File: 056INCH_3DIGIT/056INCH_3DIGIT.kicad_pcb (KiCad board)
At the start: 2 copper layers, 43.8 x 21 mm, 0 parts

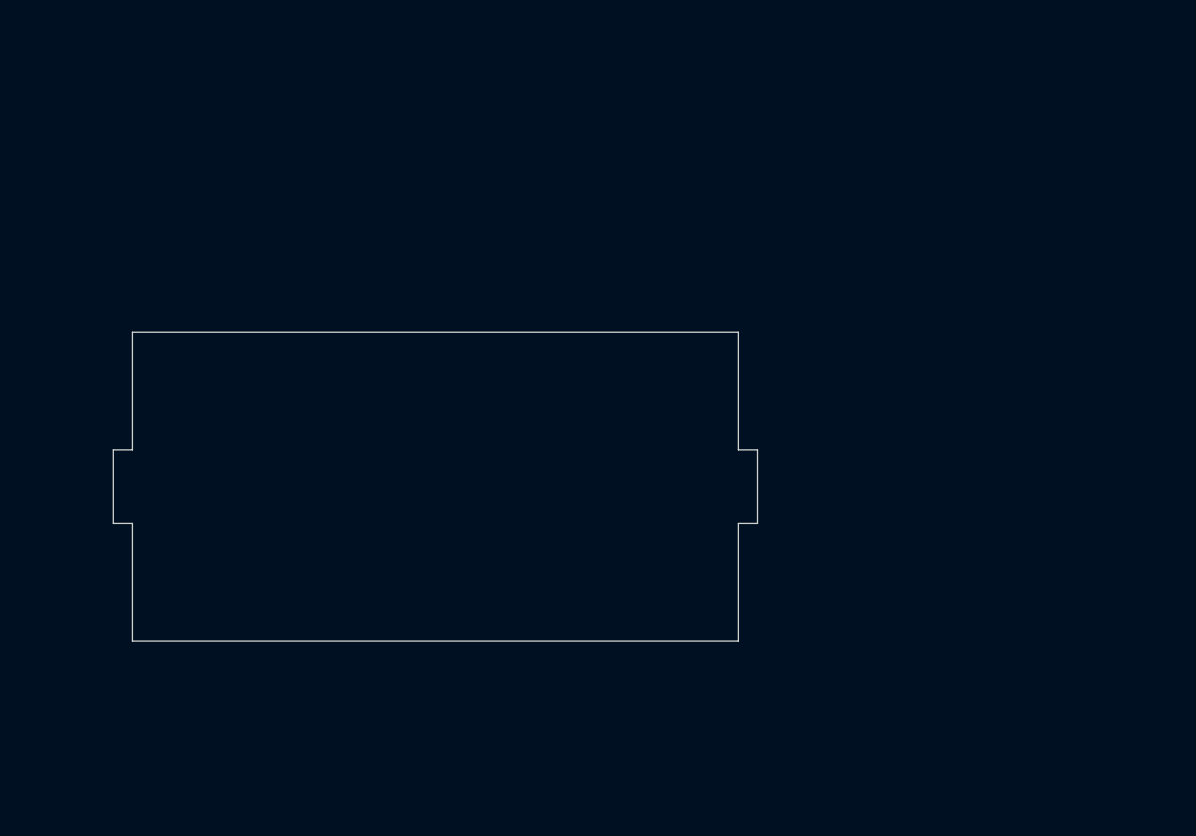
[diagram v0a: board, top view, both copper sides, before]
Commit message: halfway 3 digit display symbol
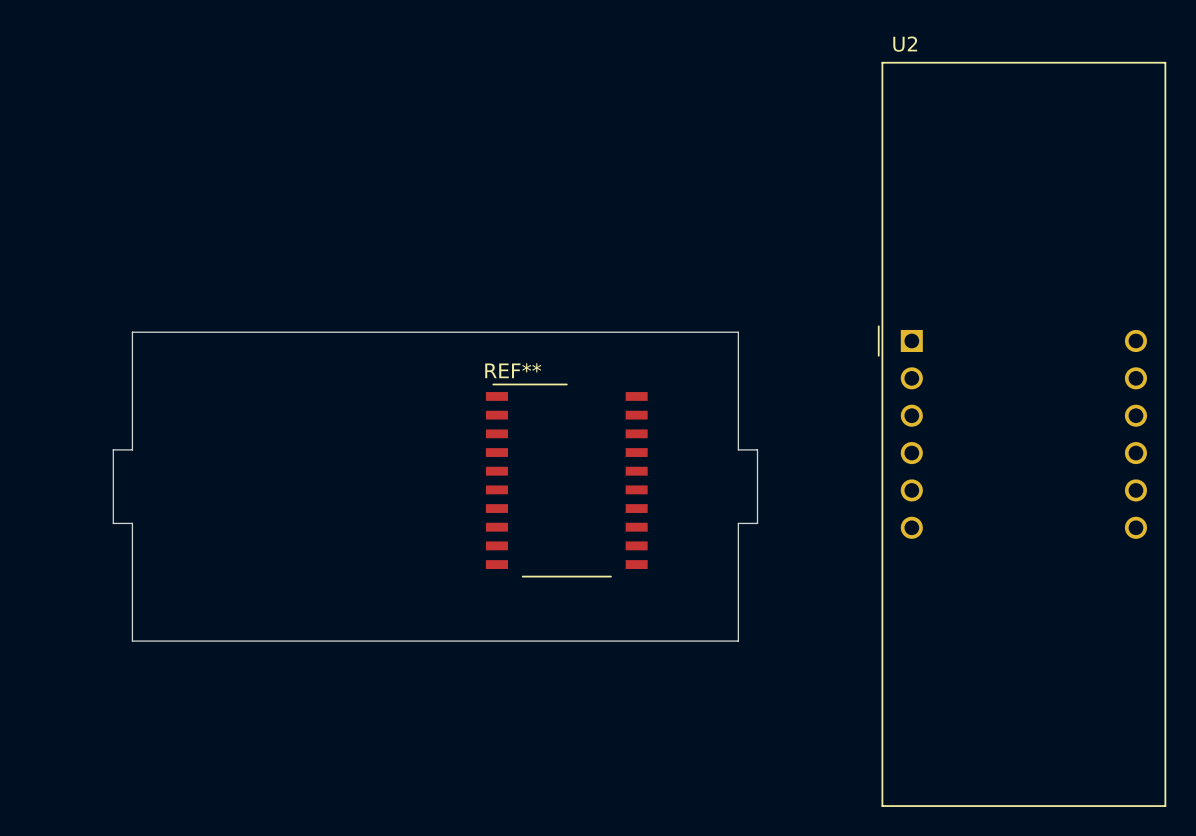
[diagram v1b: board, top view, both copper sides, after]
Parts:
- added REF**: SO-20_12.8x7.5mm_P1.27mm, Package_SO:SO-20_12.8x7.5mm_P1.27mm, F.Cu at (130.8, 110.1)
- added U2: BA56-12SRWA, KINGBRIGHTUSA:BA56-12SRWA, F.Cu at (154.3, 100.6)
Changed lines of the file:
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@@
     (tracks 0)
     (zones 0)
-    (modules 0)
-    (nets 1)
+    (modules 2)
+    (nets 13)
   )
   (page A4)
@@
   )
   (net 0 "")
+  (net 1 "Net-(U2-Pad12)")
+  (net 2 "Net-(U2-Pad11)")
+  (net 3 "Net-(U2-Pad10)")
+  (net 4 "Net-(U2-Pad9)")
+  (net 5 "Net-(U2-Pad8)")
+  (net 6 "Net-(U2-Pad7)")
+  (net 7 "Net-(U2-Pad6)")
+  (net 8 "Net-(U2-Pad5)")
+  (net 9 "Net-(U2-Pad4)")
+  (net 10 "Net-(U2-Pad3)")
+  (net 11 "Net-(U2-Pad2)")
+  (net 12 "Net-(U2-Pad1)")
   (net_class Default "This is the default net class."
     (clearance 0.2)
@@
     (uvia_dia 0.3)
     (uvia_drill 0.1)
+    (add_net "Net-(U2-Pad1)")
+    (add_net "Net-(U2-Pad10)")
+    (add_net "Net-(U2-Pad11)")
+    (add_net "Net-(U2-Pad12)")
+    (add_net "Net-(U2-Pad2)")
+    (add_net "Net-(U2-Pad3)")
+    (add_net "Net-(U2-Pad4)")
+    (add_net "Net-(U2-Pad5)")
+    (add_net "Net-(U2-Pad6)")
+    (add_net "Net-(U2-Pad7)")
+    (add_net "Net-(U2-Pad8)")
+    (add_net "Net-(U2-Pad9)")
+  )
+  (module KINGBRIGHTUSA:BA56-12SRWA (layer F.Cu)
+    (at 154.2923 100.5967)
+    (descr "3 digit 7 segment red LED, https://www.kingbrightusa.com/images/catalog/SPEC/BA56-12SRWA.pdf")
+    (tags "3 digit 7 segment red LED")
+    (fp_text reference U2 (at -0.44 -20.15) (layer F.SilkS)
+      (effects (font (size 1 1) (thickness 0.15)))
+    )
+    (fp_text value BA56-12SRWA (at 3.5 32.92) (layer F.Fab)
+      (effects (font (size 1 1) (thickness 0.15)))
+    )
+    (fp_text user %R (at 8.128 6.604) (layer F.Fab)
+      (effects (font (size 1 1) (thickness 0.15)))
+    )
+    (fp_line (start -1.88 1) (end -1.88 31.5) (layer F.Fab) (width 0.1))
+    (fp_line (start -1.88 31.5) (end 17.12 31.5) (layer F.Fab) (width 0.1))
+    (fp_line (start 17.12 -18.8) (end 17.12 31.5) (layer F.Fab) (width 0.1))
+    (fp_line (start -1.88 -18.8) (end 17.12 -18.8) (layer F.Fab) (width 0.1))
+    (fp_line (start -2.25 -1) (end -2.25 1) (layer F.SilkS) (width 0.12))
+    (fp_line (start -2.13 31.75) (end -2.13 -19.05) (layer F.CrtYd) (width 0.05))
+    (fp_line (start 17.37 31.75) (end -2.13 31.75) (layer F.CrtYd) (width 0.05))
+    (fp_line (start 17.37 -19.05) (end 17.37 31.75) (layer F.CrtYd) (width 0.05))
+    (fp_line (start -2.13 -19.05) (end 17.37 -19.05) (layer F.CrtYd) (width 0.05))
+    (fp_line (start -1.88 -1) (end -1.88 -18.8) (layer F.Fab) (width 0.1))
+    (fp_line (start -0.88 0) (end -1.88 -1) (layer F.Fab) (width 0.1))
+    (fp_line (start -1.88 1) (end -0.88 0) (layer F.Fab) (width 0.1))
+    (fp_line (start 17.24 31.62) (end 17.24 -18.92) (layer F.SilkS) (width 0.12))
+    (fp_line (start -2 31.62) (end 17.24 31.62) (layer F.SilkS) (width 0.12))
+    (fp_line (start -2 -18.92) (end -2 31.62) (layer F.SilkS) (width 0.12))
+    (fp_line (start -2 -18.92) (end 17.24 -18.92) (layer F.SilkS) (width 0.12))
+    (pad 12 thru_hole circle (at 15.24 0) (size 1.5 1.5) (drill 1) (layers *.Cu *.Mask)
+      (net 1 "Net-(U2-Pad12)"))
+    (pad 11 thru_hole circle (at 15.24 2.54) (size 1.5 1.5) (drill 1) (layers *.Cu *.Mask)
+      (net 2 "Net-(U2-Pad11)"))
+    (pad 10 thru_hole circle (at 15.24 5.08) (size 1.5 1.5) (drill 1) (layers *.Cu *.Mask)
+      (net 3 "Net-(U2-Pad10)"))
+    (pad 9 thru_hole circle (at 15.24 7.62) (size 1.5 1.5) (drill 1) (layers *.Cu *.Mask)
+      (net 4 "Net-(U2-Pad9)"))
+    (pad 8 thru_hole circle (at 15.24 10.16) (size 1.5 1.5) (drill 1) (layers *.Cu *.Mask)
+      (net 5 "Net-(U2-Pad8)"))
+    (pad 7 thru_hole circle (at 15.24 12.7) (size 1.5 1.5) (drill 1) (layers *.Cu *.Mask)
+      (net 6 "Net-(U2-Pad7)"))
+    (pad 6 thru_hole circle (at 0 12.7) (size 1.5 1.5) (drill 1) (layers *.Cu *.Mask)
+      (net 7 "Net-(U2-Pad6)"))
+    (pad 5 thru_hole circle (at 0 10.16) (size 1.5 1.5) (drill 1) (layers *.Cu *.Mask)
+      (net 8 "Net-(U2-Pad5)"))
+    (pad 4 thru_hole circle (at 0 7.62) (size 1.5 1.5) (drill 1) (layers *.Cu *.Mask)
+      (net 9 "Net-(U2-Pad4)"))
+    (pad 3 thru_hole circle (at 0 5.08) (size 1.5 1.5) (drill 1) (layers *.Cu *.Mask)
+      (net 10 "Net-(U2-Pad3)"))
+    (pad 2 thru_hole circle (at 0 2.54) (size 1.5 1.5) (drill 1) (layers *.Cu *.Mask)
+      (net 11 "Net-(U2-Pad2)"))
+    (pad 1 thru_hole rect (at 0 0) (size 1.5 1.5) (drill 1) (layers *.Cu *.Mask)
+      (net 12 "Net-(U2-Pad1)"))
+    (model ${KISYS3DMOD}/Display_7Segment.3dshapes/BA56-12SRWA.wrl
+      (at (xyz 0 0 0))
+      (scale (xyz 1 1 1))
+      (rotate (xyz 0 0 0))
+    )
+  )
+  (module Package_SO:SO-20_12.8x7.5mm_P1.27mm (layer F.Cu)
+    (at 130.8354 110.0836)
+    (descr "SO-20, 12.8x7.5mm, https://www.nxp.com/docs/en/data-sheet/SA605.pdf")
+    (tags "S0-20 ")
+    (attr smd)
+    (fp_text reference REF** (at -3.69 -7.42) (layer F.SilkS)
+      (effects (font (size 1 1) (thickness 0.15)))
+    )
+    (fp_text value SO-20_12.8x7.5mm_P1.27mm (at 0 7.99) (layer F.Fab)
+      (effects (font (size 1 1) (thickness 0.15)))
+    )
+    (fp_text user %R (at 0 0) (layer F.Fab)
+      (effects (font (size 1 1) (thickness 0.15)))
+    )
+    (fp_line (start -5.7 6.7) (end -5.7 -6.7) (layer F.CrtYd) (width 0.05))
+    (fp_line (start 5.7 6.7) (end -5.7 6.7) (layer F.CrtYd) (width 0.05))
+    (fp_line (start 5.7 -6.7) (end 5.7 6.7) (layer F.CrtYd) (width 0.05))
+    (fp_line (start -5.7 -6.7) (end 5.7 -6.7) (layer F.CrtYd) (width 0.05))
+    (fp_line (start -5 -6.53) (end 0 -6.53) (layer F.SilkS) (width 0.12))
+    (fp_line (start -3 6.53) (end 3 6.53) (layer F.SilkS) (width 0.12))
+    (fp_line (start -2.2 -5.4) (end -1.2 -6.4) (layer F.Fab) (width 0.1))
+    (fp_line (start -2.2 6.4) (end -2.2 -5.4) (layer F.Fab) (width 0.1))
+    (fp_line (start 2.2 6.4) (end -2.2 6.4) (layer F.Fab) (width 0.1))
+    (fp_line (start 2.2 -6.4) (end 2.2 6.4) (layer F.Fab) (width 0.1))
+    (fp_line (start -1.2 -6.4) (end 2.2 -6.4) (layer F.Fab) (width 0.1))
+    (pad 20 smd rect (at 4.75 -5.715) (size 1.5 0.6) (layers F.Cu F.Paste F.Mask))
+    (pad 19 smd rect (at 4.75 -4.445) (size 1.5 0.6) (layers F.Cu F.Paste F.Mask))
+    (pad 18 smd rect (at 4.75 -3.175) (size 1.5 0.6) (layers F.Cu F.Paste F.Mask))
+    (pad 17 smd rect (at 4.75 -1.905) (size 1.5 0.6) (layers F.Cu F.Paste F.Mask))
+    (pad 16 smd rect (at 4.75 -0.635) (size 1.5 0.6) (layers F.Cu F.Paste F.Mask))
+    (pad 15 smd rect (at 4.75 0.635) (size 1.5 0.6) (layers F.Cu F.Paste F.Mask))
+    (pad 14 smd rect (at 4.75 1.905) (size 1.5 0.6) (layers F.Cu F.Paste F.Mask))
+    (pad 13 smd rect (at 4.75 3.175) (size 1.5 0.6) (layers F.Cu F.Paste F.Mask))
+    (pad 12 smd rect (at 4.75 4.445) (size 1.5 0.6) (layers F.Cu F.Paste F.Mask))
+    (pad 11 smd rect (at 4.75 5.715) (size 1.5 0.6) (layers F.Cu F.Paste F.Mask))
+    (pad 10 smd rect (at -4.75 5.715) (size 1.5 0.6) (layers F.Cu F.Paste F.Mask))
+    (pad 9 smd rect (at -4.75 4.445) (size 1.5 0.6) (layers F.Cu F.Paste F.Mask))
+    (pad 8 smd rect (at -4.75 3.175) (size 1.5 0.6) (layers F.Cu F.Paste F.Mask))
+    (pad 7 smd rect (at -4.75 1.905) (size 1.5 0.6) (layers F.Cu F.Paste F.Mask))
+    (pad 1 smd rect (at -4.75 -5.715) (size 1.5 0.6) (layers F.Cu F.Paste F.Mask))
+    (pad 2 smd rect (at -4.75 -4.445) (size 1.5 0.6) (layers F.Cu F.Paste F.Mask))
+    (pad 3 smd rect (at -4.75 -3.175) (size 1.5 0.6) (layers F.Cu F.Paste F.Mask))
+    (pad 4 smd rect (at -4.75 -1.905) (size 1.5 0.6) (layers F.Cu F.Paste F.Mask))
+    (pad 5 smd rect (at -4.75 -0.635) (size 1.5 0.6) (layers F.Cu F.Paste F.Mask))
+    (pad 6 smd rect (at -4.75 0.635) (size 1.5 0.6) (layers F.Cu F.Paste F.Mask))
+    (model ${KISYS3DMOD}/Package_SO.3dshapes/SO-20_12.8x7.5mm_P1.27mm.wrl
+      (at (xyz 0 0 0))
+      (scale (xyz 1 1 1))
+      (rotate (xyz 0 0 0))
+    )
   )
   (gr_line (start 142.5 113) (end 142.5 121) (layer Edge.Cuts) (width 0.05))

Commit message: 3 digit display symbol & footprint finished
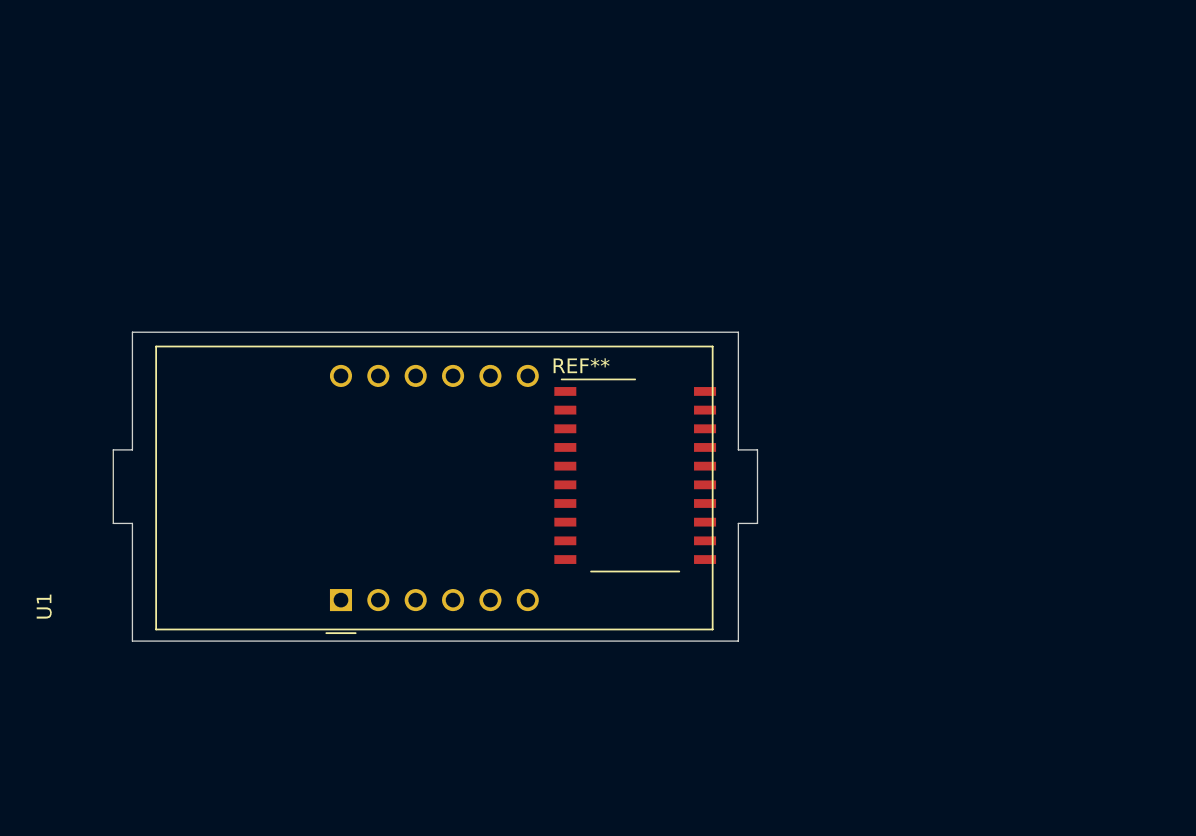
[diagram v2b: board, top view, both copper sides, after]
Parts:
- removed U2: BA56-12SRWA, KINGBRIGHTUSA:BA56-12SRWA
- added U1: BA56-12SRWA, KINGBRIGHTUSA:BA56-12SRWA, F.Cu at (115.5, 118.2)
- moved REF** 4.66 mm to (135.5, 109.7)
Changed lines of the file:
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@@
   )
   (net 0 "")
-  (net 1 "Net-(U2-Pad12)")
-  (net 2 "Net-(U2-Pad11)")
-  (net 3 "Net-(U2-Pad10)")
-  (net 4 "Net-(U2-Pad9)")
-  (net 5 "Net-(U2-Pad8)")
-  (net 6 "Net-(U2-Pad7)")
-  (net 7 "Net-(U2-Pad6)")
-  (net 8 "Net-(U2-Pad5)")
-  (net 9 "Net-(U2-Pad4)")
-  (net 10 "Net-(U2-Pad3)")
-  (net 11 "Net-(U2-Pad2)")
-  (net 12 "Net-(U2-Pad1)")
+  (net 1 "Net-(U1-Pad12)")
+  (net 2 "Net-(U1-Pad11)")
+  (net 3 "Net-(U1-Pad10)")
+  (net 4 "Net-(U1-Pad9)")
+  (net 5 "Net-(U1-Pad8)")
+  (net 6 "Net-(U1-Pad7)")
+  (net 7 "Net-(U1-Pad6)")
+  (net 8 "Net-(U1-Pad5)")
+  (net 9 "Net-(U1-Pad4)")
+  (net 10 "Net-(U1-Pad3)")
+  (net 11 "Net-(U1-Pad2)")
+  (net 12 "Net-(U1-Pad1)")
   (net_class Default "This is the default net class."
     (clearance 0.2)
@@
     (uvia_dia 0.3)
     (uvia_drill 0.1)
-    (add_net "Net-(U2-Pad1)")
-    (add_net "Net-(U2-Pad10)")
-    (add_net "Net-(U2-Pad11)")
-    (add_net "Net-(U2-Pad12)")
-    (add_net "Net-(U2-Pad2)")
-    (add_net "Net-(U2-Pad3)")
-    (add_net "Net-(U2-Pad4)")
-    (add_net "Net-(U2-Pad5)")
-    (add_net "Net-(U2-Pad6)")
-    (add_net "Net-(U2-Pad7)")
-    (add_net "Net-(U2-Pad8)")
-    (add_net "Net-(U2-Pad9)")
+    (add_net "Net-(U1-Pad1)")
+    (add_net "Net-(U1-Pad10)")
+    (add_net "Net-(U1-Pad11)")
+    (add_net "Net-(U1-Pad12)")
+    (add_net "Net-(U1-Pad2)")
+    (add_net "Net-(U1-Pad3)")
+    (add_net "Net-(U1-Pad4)")
+    (add_net "Net-(U1-Pad5)")
+    (add_net "Net-(U1-Pad6)")
+    (add_net "Net-(U1-Pad7)")
+    (add_net "Net-(U1-Pad8)")
+    (add_net "Net-(U1-Pad9)")
   )
   (module KINGBRIGHTUSA:BA56-12SRWA (layer F.Cu)
-    (at 154.2923 100.5967)
+    (at 115.4811 118.2116 90)
     (descr "3 digit 7 segment red LED, https://www.kingbrightusa.com/images/catalog/SPEC/BA56-12SRWA.pdf")
     (tags "3 digit 7 segment red LED")
-    (fp_text reference U2 (at -0.44 -20.15) (layer F.SilkS)
+    (fp_text reference U1 (at -0.44 -20.15 90) (layer F.SilkS)
       (effects (font (size 1 1) (thickness 0.15)))
     )
-    (fp_text value BA56-12SRWA (at 3.5 32.92) (layer F.Fab)
+    (fp_text value BA56-12SRWA (at 3.5 32.92 90) (layer F.Fab)
       (effects (font (size 1 1) (thickness 0.15)))
     )
-    (fp_text user %R (at 8.128 6.604) (layer F.Fab)
+    (fp_text user %R (at 8.128 6.604 90) (layer F.Fab)
       (effects (font (size 1 1) (thickness 0.15)))
     )
-    (fp_line (start -1.88 1) (end -1.88 31.5) (layer F.Fab) (width 0.1))
-    (fp_line (start -1.88 31.5) (end 17.12 31.5) (layer F.Fab) (width 0.1))
-    (fp_line (start 17.12 -18.8) (end 17.12 31.5) (layer F.Fab) (width 0.1))
-    (fp_line (start -1.88 -18.8) (end 17.12 -18.8) (layer F.Fab) (width 0.1))
+    (fp_line (start -1.88 1) (end -1.88 25.15) (layer F.Fab) (width 0.1))
+    (fp_line (start -1.88 25.15) (end 17.12 25.15) (layer F.Fab) (width 0.1))
+    (fp_line (start 17.12 -12.45) (end 17.12 25.15) (layer F.Fab) (width 0.1))
+    (fp_line (start -1.88 -12.45) (end 17.12 -12.45) (layer F.Fab) (width 0.1))
     (fp_line (start -2.25 -1) (end -2.25 1) (layer F.SilkS) (width 0.12))
-    (fp_line (start -2.13 31.75) (end -2.13 -19.05) (layer F.CrtYd) (width 0.05))
-    (fp_line (start 17.37 31.75) (end -2.13 31.75) (layer F.CrtYd) (width 0.05))
-    (fp_line (start 17.37 -19.05) (end 17.37 31.75) (layer F.CrtYd) (width 0.05))
-    (fp_line (start -2.13 -19.05) (end 17.37 -19.05) (layer F.CrtYd) (width 0.05))
-    (fp_line (start -1.88 -1) (end -1.88 -18.8) (layer F.Fab) (width 0.1))
+    (fp_line (start -2.13 25.4) (end -2.13 -12.7) (layer F.CrtYd) (width 0.05))
+    (fp_line (start 17.37 25.4) (end -2.13 25.4) (layer F.CrtYd) (width 0.05))
+    (fp_line (start 17.37 -12.7) (end 17.37 25.4) (layer F.CrtYd) (width 0.05))
+    (fp_line (start -2.13 -12.7) (end 17.37 -12.7) (layer F.CrtYd) (width 0.05))
+    (fp_line (start -1.88 -1) (end -1.88 -12.45) (layer F.Fab) (width 0.1))
     (fp_line (start -0.88 0) (end -1.88 -1) (layer F.Fab) (width 0.1))
     (fp_line (start -1.88 1) (end -0.88 0) (layer F.Fab) (width 0.1))
-    (fp_line (start 17.24 31.62) (end 17.24 -18.92) (layer F.SilkS) (width 0.12))
-    (fp_line (start -2 31.62) (end 17.24 31.62) (layer F.SilkS) (width 0.12))
-    (fp_line (start -2 -18.92) (end -2 31.62) (layer F.SilkS) (width 0.12))
-    (fp_line (start -2 -18.92) (end 17.24 -18.92) (layer F.SilkS) (width 0.12))
-    (pad 12 thru_hole circle (at 15.24 0) (size 1.5 1.5) (drill 1) (layers *.Cu *.Mask)
-      (net 1 "Net-(U2-Pad12)"))
-    (pad 11 thru_hole circle (at 15.24 2.54) (size 1.5 1.5) (drill 1) (layers *.Cu *.Mask)
-      (net 2 "Net-(U2-Pad11)"))
-    (pad 10 thru_hole circle (at 15.24 5.08) (size 1.5 1.5) (drill 1) (layers *.Cu *.Mask)
-      (net 3 "Net-(U2-Pad10)"))
-    (pad 9 thru_hole circle (at 15.24 7.62) (size 1.5 1.5) (drill 1) (layers *.Cu *.Mask)
-      (net 4 "Net-(U2-Pad9)"))
-    (pad 8 thru_hole circle (at 15.24 10.16) (size 1.5 1.5) (drill 1) (layers *.Cu *.Mask)
-      (net 5 "Net-(U2-Pad8)"))
-    (pad 7 thru_hole circle (at 15.24 12.7) (size 1.5 1.5) (drill 1) (layers *.Cu *.Mask)
-      (net 6 "Net-(U2-Pad7)"))
-    (pad 6 thru_hole circle (at 0 12.7) (size 1.5 1.5) (drill 1) (layers *.Cu *.Mask)
-      (net 7 "Net-(U2-Pad6)"))
-    (pad 5 thru_hole circle (at 0 10.16) (size 1.5 1.5) (drill 1) (layers *.Cu *.Mask)
-      (net 8 "Net-(U2-Pad5)"))
-    (pad 4 thru_hole circle (at 0 7.62) (size 1.5 1.5) (drill 1) (layers *.Cu *.Mask)
-      (net 9 "Net-(U2-Pad4)"))
-    (pad 3 thru_hole circle (at 0 5.08) (size 1.5 1.5) (drill 1) (layers *.Cu *.Mask)
-      (net 10 "Net-(U2-Pad3)"))
-    (pad 2 thru_hole circle (at 0 2.54) (size 1.5 1.5) (drill 1) (layers *.Cu *.Mask)
-      (net 11 "Net-(U2-Pad2)"))
-    (pad 1 thru_hole rect (at 0 0) (size 1.5 1.5) (drill 1) (layers *.Cu *.Mask)
-      (net 12 "Net-(U2-Pad1)"))
+    (fp_line (start 17.24 25.27) (end 17.24 -12.57) (layer F.SilkS) (width 0.12))
+    (fp_line (start -2 25.27) (end 17.24 25.27) (layer F.SilkS) (width 0.12))
+    (fp_line (start -2 -12.57) (end -2 25.27) (layer F.SilkS) (width 0.12))
+    (fp_line (start -2 -12.57) (end 17.24 -12.57) (layer F.SilkS) (width 0.12))
+    (pad 12 thru_hole circle (at 15.24 0 90) (size 1.5 1.5) (drill 1) (layers *.Cu *.Mask)
+      (net 1 "Net-(U1-Pad12)"))
+    (pad 11 thru_hole circle (at 15.24 2.54 90) (size 1.5 1.5) (drill 1) (layers *.Cu *.Mask)
+      (net 2 "Net-(U1-Pad11)"))
+    (pad 10 thru_hole circle (at 15.24 5.08 90) (size 1.5 1.5) (drill 1) (layers *.Cu *.Mask)
+      (net 3 "Net-(U1-Pad10)"))
+    (pad 9 thru_hole circle (at 15.24 7.62 90) (size 1.5 1.5) (drill 1) (layers *.Cu *.Mask)
+      (net 4 "Net-(U1-Pad9)"))
+    (pad 8 thru_hole circle (at 15.24 10.16 90) (size 1.5 1.5) (drill 1) (layers *.Cu *.Mask)
+      (net 5 "Net-(U1-Pad8)"))
+    (pad 7 thru_hole circle (at 15.24 12.7 90) (size 1.5 1.5) (drill 1) (layers *.Cu *.Mask)
+      (net 6 "Net-(U1-Pad7)"))
+    (pad 6 thru_hole circle (at 0 12.7 90) (size 1.5 1.5) (drill 1) (layers *.Cu *.Mask)
+      (net 7 "Net-(U1-Pad6)"))
+    (pad 5 thru_hole circle (at 0 10.16 90) (size 1.5 1.5) (drill 1) (layers *.Cu *.Mask)
+      (net 8 "Net-(U1-Pad5)"))
+    (pad 4 thru_hole circle (at 0 7.62 90) (size 1.5 1.5) (drill 1) (layers *.Cu *.Mask)
+      (net 9 "Net-(U1-Pad4)"))
+    (pad 3 thru_hole circle (at 0 5.08 90) (size 1.5 1.5) (drill 1) (layers *.Cu *.Mask)
+      (net 10 "Net-(U1-Pad3)"))
+    (pad 2 thru_hole circle (at 0 2.54 90) (size 1.5 1.5) (drill 1) (layers *.Cu *.Mask)
+      (net 11 "Net-(U1-Pad2)"))
+    (pad 1 thru_hole rect (at 0 0 90) (size 1.5 1.5) (drill 1) (layers *.Cu *.Mask)
+      (net 12 "Net-(U1-Pad1)"))
     (model ${KISYS3DMOD}/Display_7Segment.3dshapes/BA56-12SRWA.wrl
       (at (xyz 0 0 0))
@@
   )
   (module Package_SO:SO-20_12.8x7.5mm_P1.27mm (layer F.Cu)
-    (at 130.8354 110.0836)
+    (at 135.4836 109.7407)
     (descr "SO-20, 12.8x7.5mm, https://www.nxp.com/docs/en/data-sheet/SA605.pdf")
     (tags "S0-20 ")
